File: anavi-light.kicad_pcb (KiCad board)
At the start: 2 copper layers, 65 x 30 mm, 24 parts, among them Q1 IRF8721PBF-1, Q2 IRF8721PBF-1, Q3 IRF8721PBF-1, U1 CAT24C32WI-GT3

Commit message: anavi-light: Fixes
Suggested-by: Rangel Ivanov <rangelivanov88@gmail.com>
Signed-off-by: Leon Anavi <leon@anavi.org>
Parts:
- DC1: value dc_jack -> 12V
- moved PIR 0.51 mm to (151.9, 90.0)
- renumbered PIR1 to PIR
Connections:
- DC1 pad 1: Net-(DC1-Pad1) -> GND
- DC1 pad 2: Net-(DC1-Pad1) -> GND
- DC1 pad 3: GND -> Net-(DC1-Pad3)
- RGB1 pad 1: Net-(DC1-Pad1) -> Net-(DC1-Pad3)
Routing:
- net Net-(DC1-Pad3): track 0.00 -> 35.5 mm
- net Net-(DC1-Pad1): track 29.8 -> 0.00 mm
- net +3V3: track 43.5 -> 67.1 mm, vias 2 -> 3
- net Net-(Q3-Pad5): track 13.4 -> 17.4 mm
- net Net-(Q2-Pad5): track 22.9 -> 26.7 mm
- net Net-(Q1-Pad5): track 27.0 -> 30.8 mm
- net Net-(R7-Pad2): track 42.2 -> 43.7 mm
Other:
- board text added: "5V OUT GND"

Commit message: Adjust labels on front silkscreen
Signed-off-by: Leon Anavi <leon@anavi.org>
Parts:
- RGB1: footprint Terminal_Blocks:TerminalBlock_Pheonix_MKDS1.5-4pol -> myfootprint:TerminalBlock_4PIN
- renumbered R6 to R4, R7 to R5
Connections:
- R4 pad 2: Net-(R6-Pad2) -> (no net)
- R5 pad 2: Net-(R7-Pad2) -> (no net)
- RASP_CONN1 pad 3: Net-(R6-Pad2) -> Net-(R4-Pad2)
- RASP_CONN1 pad 5: Net-(R7-Pad2) -> Net-(R5-Pad2)
- SENS1 pad 3: Net-(R7-Pad2) -> Net-(R5-Pad2)
- SENS1 pad 4: Net-(R6-Pad2) -> Net-(R4-Pad2)
- SENS2 pad 3: Net-(R7-Pad2) -> Net-(R5-Pad2)
- SENS2 pad 4: Net-(R6-Pad2) -> Net-(R4-Pad2)
- SENS3 pad 3: Net-(R7-Pad2) -> Net-(R5-Pad2)
- SENS3 pad 4: Net-(R6-Pad2) -> Net-(R4-Pad2)
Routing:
- net Net-(R7-Pad2): track 43.7 -> 0.00 mm, vias 1 -> 0
- net Net-(R5-Pad2): track 0.00 -> 43.7 mm, vias 0 -> 1
- net Net-(R6-Pad2): track 41.3 -> 0.00 mm
- net Net-(R4-Pad2): track 0.00 -> 41.3 mm
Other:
- board text added: "12V GREEN RED BLUE"

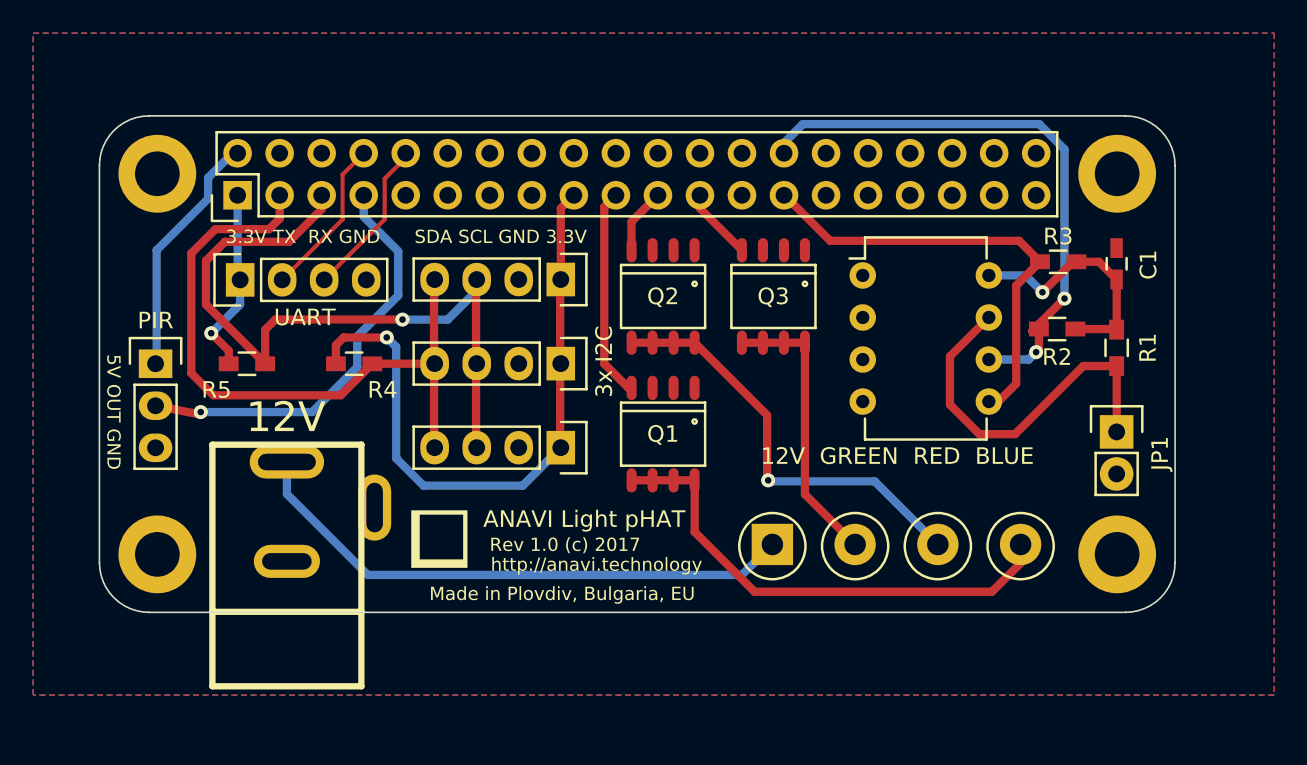
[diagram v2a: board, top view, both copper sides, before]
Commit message: anavi-light.kicad_pcb: Improve routing
Signed-off-by: Leon Anavi <leon@anavi.org>
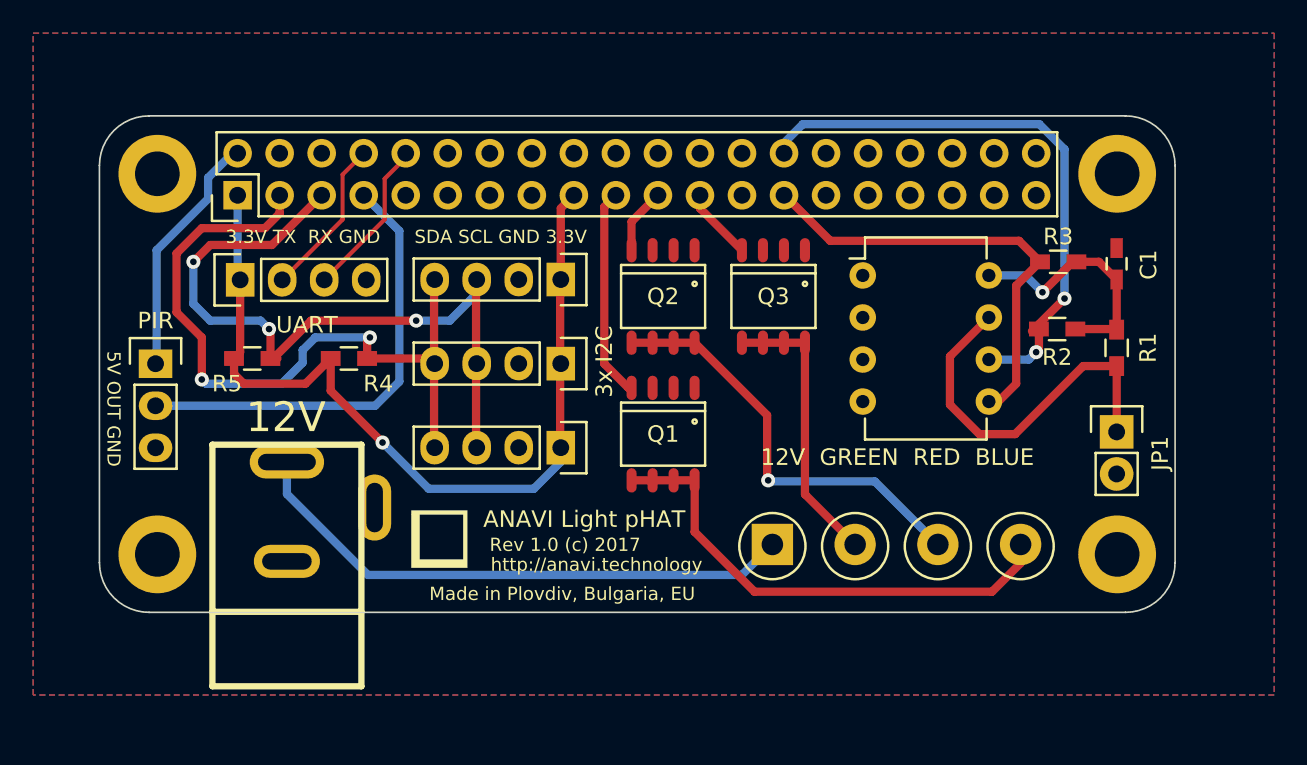
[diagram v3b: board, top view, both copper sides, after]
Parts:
- moved R4 0.45 mm to (163.6, 89.7)
- moved R5 0.45 mm to (157.7, 89.7)
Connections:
- R4 pad 2: (no net) -> Net-(R4-Pad2)
- R5 pad 2: (no net) -> Net-(R5-Pad2)
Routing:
- net Net-(R4-Pad2): track 41.3 -> 45.0 mm, vias 0 -> 2
- net +3V3: track 67.1 -> 69.7 mm, vias 3 -> 2
- net Net-(PIR1-Pad2): track 26.4 -> 28.2 mm, vias 1 -> 0
- net Net-(R5-Pad2): track 43.7 -> 45.4 mm, vias 1 -> 3

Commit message: Add MOSFET gate resistors
Signed-off-by: Leon Anavi <leon@anavi.org>
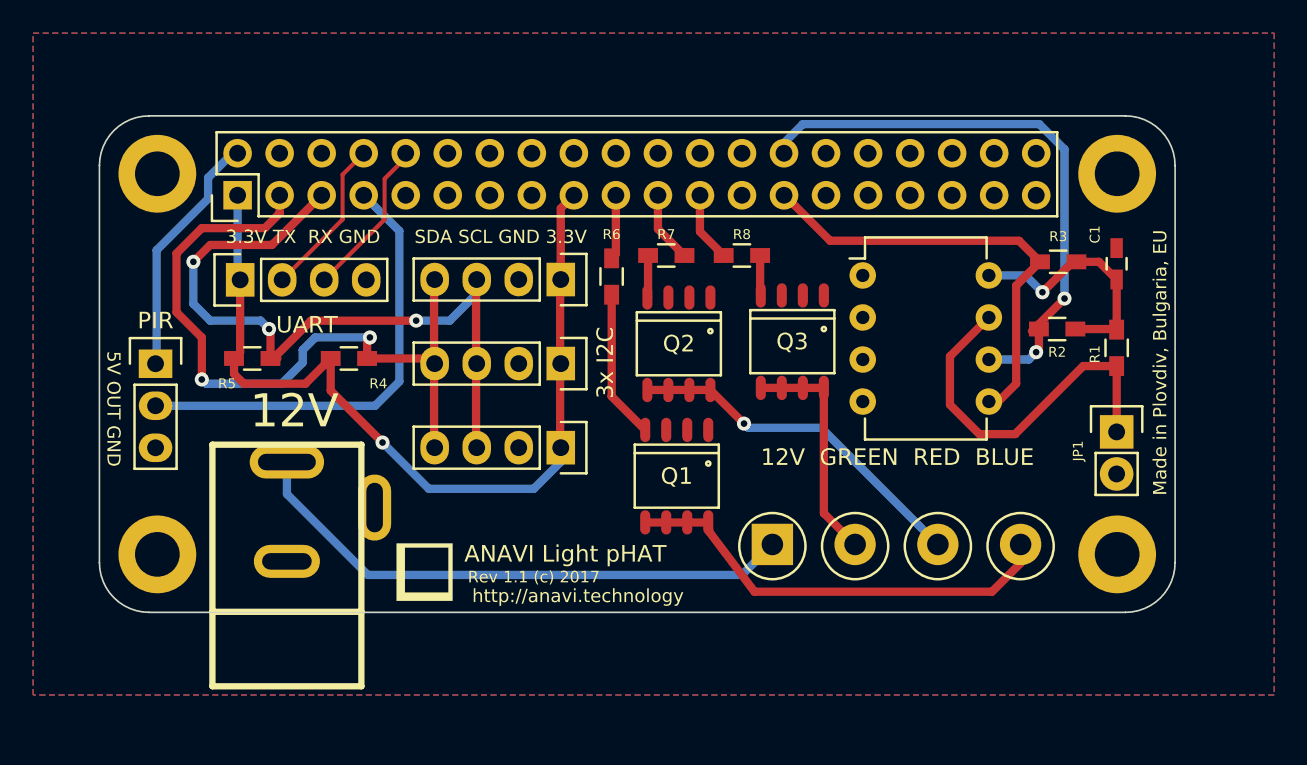
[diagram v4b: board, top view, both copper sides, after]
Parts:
- added R6: 220R, Resistors_SMD:R_0603_HandSoldering, F.Cu at (179.5, 84.7)
- added R7: 220R, Resistors_SMD:R_0603_HandSoldering, F.Cu at (182.8, 83.4)
- added R8: 220R, Resistors_SMD:R_0603_HandSoldering, F.Cu at (187.3, 83.4)
- DC1: value 12V -> dc_jack
- moved Q2 3.01 mm to (183.5, 88.8)
- moved Q3 2.96 mm to (190.4, 88.6)
- moved Q1 2.67 mm to (183.4, 96.8)
- moved ? 2.19 mm to (168.1, 102.6)
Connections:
- RASP_CONN1 pad 19: Net-(Q1-Pad4) -> Net-(R6-Pad2)
- RASP_CONN1 pad 21: Net-(Q2-Pad4) -> Net-(R7-Pad2)
- RASP_CONN1 pad 23: Net-(Q3-Pad4) -> Net-(R8-Pad2)
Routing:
- net Net-(Q2-Pad5): track 26.7 -> 21.8 mm
- net Net-(R7-Pad2): track 0.00 -> 4.30 mm
- net Net-(R8-Pad2): track 0.00 -> 4.23 mm
- net Net-(R6-Pad2): track 0.00 -> 3.92 mm
- net Net-(Q1-Pad4): track 12.7 -> 9.01 mm
- net Net-(Q3-Pad5): track 17.4 -> 14.2 mm
- net Net-(Q1-Pad5): track 30.8 -> 27.7 mm
- net Net-(Q3-Pad4): track 4.37 -> 2.43 mm
- net Net-(Q2-Pad4): track 3.98 -> 2.56 mm
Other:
- board text added: "12V"
- board text added: "Rev 1.1 (c) 2017"
- board text removed: "Rev 1.0 (c) 2017"
